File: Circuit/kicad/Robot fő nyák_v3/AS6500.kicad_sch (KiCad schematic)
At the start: 12 parts, among them U49 AS6500-FQFM, Y3 5MHz

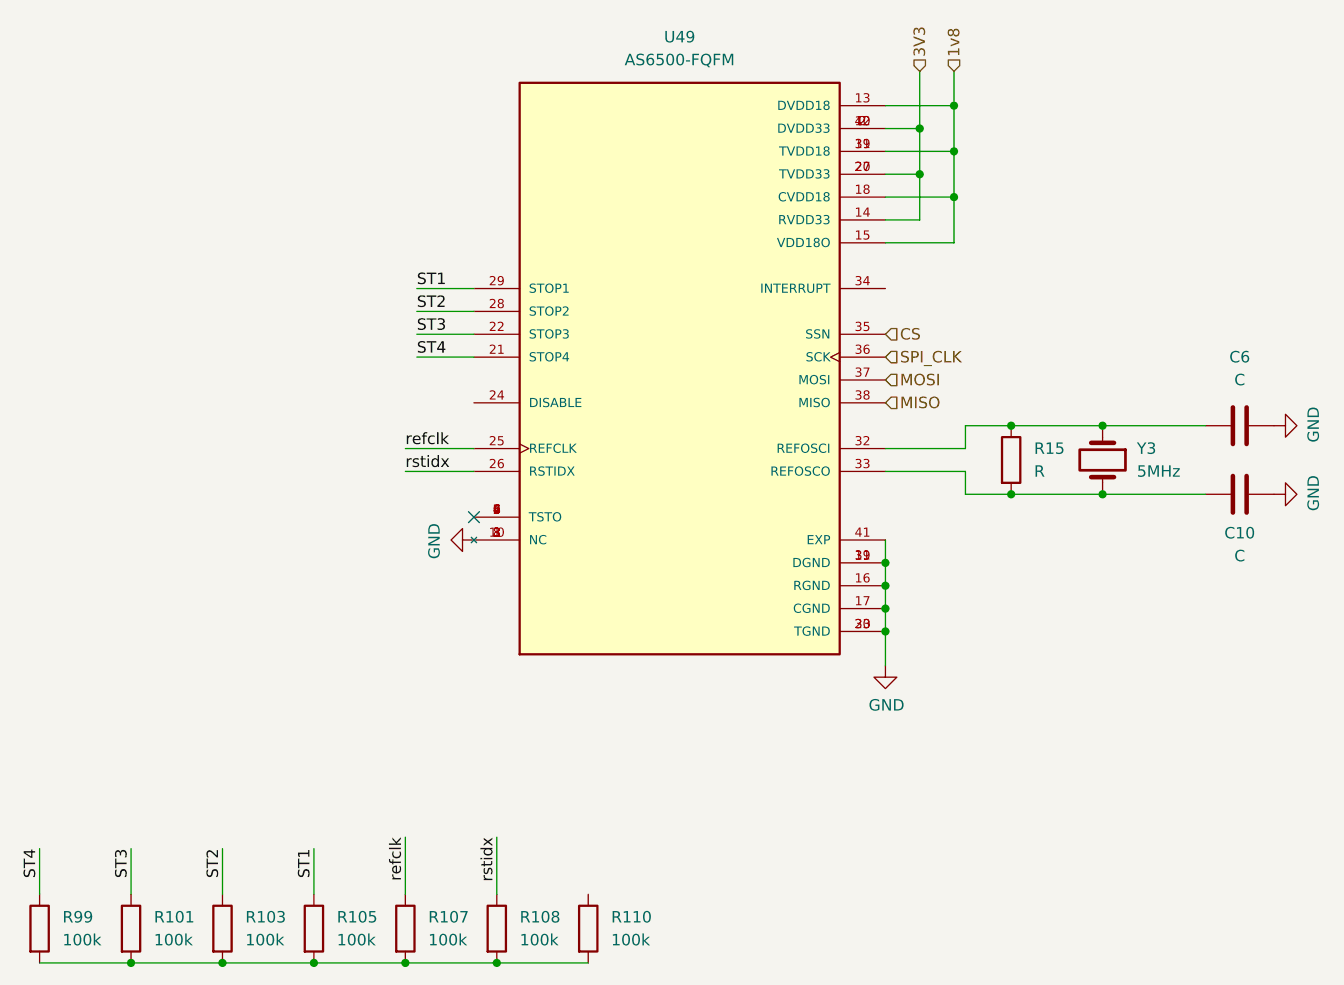
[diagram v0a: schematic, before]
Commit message: kicad v0.1 footprint- assing spi finish
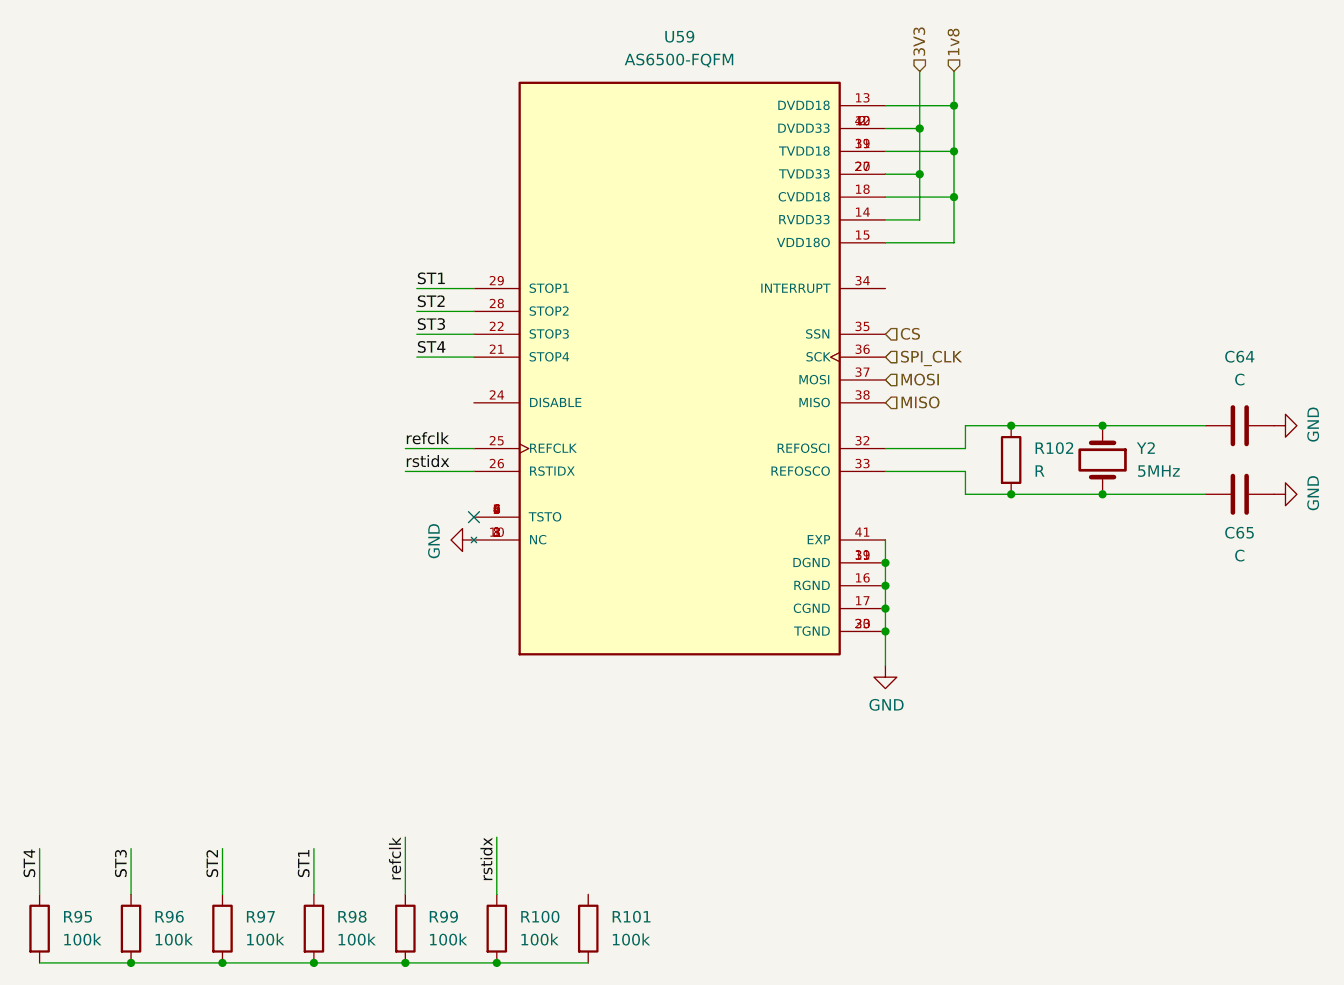
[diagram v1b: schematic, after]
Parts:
- C64: renamed from C6; footprint (none) -> Capacitor_SMD:C_0805_2012Metric
- C65: renamed from C10; footprint (none) -> Capacitor_SMD:C_0805_2012Metric
- R100: renamed from R108; footprint (none) -> Resistor_SMD:R_0805_2012Metric
- R101: renamed from R110; footprint (none) -> Resistor_SMD:R_0805_2012Metric
- R102: renamed from R15; footprint (none) -> Resistor_SMD:R_0805_2012Metric
- R95: renamed from R99; footprint (none) -> Resistor_SMD:R_0805_2012Metric
- R96: renamed from R101; footprint (none) -> Resistor_SMD:R_0805_2012Metric
- R97: renamed from R103; footprint (none) -> Resistor_SMD:R_0805_2012Metric
- R98: renamed from R105; footprint (none) -> Resistor_SMD:R_0805_2012Metric
- R99: renamed from R107; footprint (none) -> Resistor_SMD:R_0805_2012Metric
- Y2: renamed from Y3; footprint (none) -> Crystal:Crystal_SMD_HC49-SD
- renumbered U49 to U59

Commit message: kicad update new readme media updates the circuit is 95% finished
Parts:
- renumbered R102 to R100, R95 to R25, R96 to R27, R97 to R95, R98 to R96, R99 to R97, R100 to R98, R101 to R99
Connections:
- net DIS: now reaches U59.24 (DISABLE)
- no-connect marks 1 -> 2
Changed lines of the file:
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@@
+	)
+	(no_connect
+		(at 111.76 50.8)
 	)
 	(no_connect
@@
 	(wire
 		(pts
-			(xy 59.69 53.34) (xy 66.04 53.34)
+			(xy 49.53 53.34) (xy 66.04 53.34)
 		)
 		(stroke
@@
 	(wire
 		(pts
-			(xy 59.69 55.88) (xy 66.04 55.88)
+			(xy 49.53 55.88) (xy 66.04 55.88)
 		)
 		(stroke
@@
 	(wire
 		(pts
-			(xy 59.69 58.42) (xy 66.04 58.42)
+			(xy 49.53 58.42) (xy 66.04 58.42)
 		)
 		(stroke
@@
 	(wire
 		(pts
-			(xy 59.69 50.8) (xy 66.04 50.8)
+			(xy 49.53 50.8) (xy 66.04 50.8)
 		)
 		(stroke
@@
 		(pts
 			(xy 115.57 38.1) (xy 115.57 33.02)
+		)
+		(stroke
+			(width 0)
+			(type default)
+		)
+	)
+	(wire
+		(pts
+			(xy 58.42 63.5) (xy 66.04 63.5)
 		)
 		(stroke
@@
 	)
 	(label "ST2"
-		(at 59.69 53.34 0)
+		(at 49.53 53.34 0)
 		(effects
 			(font
@@
 	)
 	(label "ST3"
-		(at 59.69 55.88 0)
+		(at 49.53 55.88 0)
 		(effects
 			(font
@@
 	)
 	(label "ST1"
-		(at 59.69 50.8 0)
+		(at 49.53 50.8 0)
 		(effects
 			(font
@@
 		)
 	)
+	(label "DIS"
+		(at 58.42 63.5 0)
+		(effects
+			(font
+				(size 1.27 1.27)
+			)
+			(justify left bottom)
+		)
+	)
 	(label "ST4"
-		(at 59.69 58.42 0)
+		(at 49.53 58.42 0)
 		(effects
 			(font
@@
 		(dnp no)
 		(fields_autoplaced yes)
-		(property "Reference" "R97"
+		(property "Reference" "R95"
 			(at 40.64 120.6499 0)
 			(effects
@@
 		(instances
 			(project "CM5IO"
-				(path "/e63e39d7-6ac0-4ffd-8aa3-1841a4541b55/a83afe30-5c7e-43cb-a5b2-f6f97a0812b3/86209e6a-92ae-4699-a125-02d46b525fc7/cb22f4d7-edd9-44f2-99e1-8067511610b0"
-					(reference "R97")
+				(path "/e63e39d7-6ac0-4ffd-8aa3-1841a4541b55/a83afe30-5c7e-43cb-a5b2-f6f97a0812b3/86209e6a-92ae-4699-a125-02d46b525fc7/e7466be3-9271-431f-82f5-a7a34fd4d93a"
+					(reference "R95")
 					(unit 1)
 				)
@@
 		(instances
 			(project "CM5IO"
-				(path "/e63e39d7-6ac0-4ffd-8aa3-1841a4541b55/a83afe30-5c7e-43cb-a5b2-f6f97a0812b3/86209e6a-92ae-4699-a125-02d46b525fc7/cb22f4d7-edd9-44f2-99e1-8067511610b0"
+				(path "/e63e39d7-6ac0-4ffd-8aa3-1841a4541b55/a83afe30-5c7e-43cb-a5b2-f6f97a0812b3/86209e6a-92ae-4699-a125-02d46b525fc7/e7466be3-9271-431f-82f5-a7a34fd4d93a"
 					(reference "C65")
 					(unit 1)
@@
 		(dnp no)
 		(fields_autoplaced yes)
-		(property "Reference" "R100"
+		(property "Reference" "R98"
 			(at 71.12 120.6499 0)
 			(effects
@@
 		(instances
 			(project "CM5IO"
-				(path "/e63e39d7-6ac0-4ffd-8aa3-1841a4541b55/a83afe30-5c7e-43cb-a5b2-f6f97a0812b3/86209e6a-92ae-4699-a125-02d46b525fc7/cb22f4d7-edd9-44f2-99e1-8067511610b0"
-					(reference "R100")
+				(path "/e63e39d7-6ac0-4ffd-8aa3-1841a4541b55/a83afe30-5c7e-43cb-a5b2-f6f97a0812b3/86209e6a-92ae-4699-a125-02d46b525fc7/e7466be3-9271-431f-82f5-a7a34fd4d93a"
+					(reference "R98")
 					(unit 1)
 				)
@@
 		(dnp no)
 		(fields_autoplaced yes)
-		(property "Reference" "R102"
+		(property "Reference" "R100"
 			(at 128.27 68.5799 0)
 			(effects
@@
 		)
 		(instances
-			(project ""
-				(path "/e63e39d7-6ac0-4ffd-8aa3-1841a4541b55/a83afe30-5c7e-43cb-a5b2-f6f97a0812b3/86209e6a-92ae-4699-a125-02d46b525fc7/160ccd78-386a-4b8b-89f3-6c9a73a758a1"
-					(reference "R?")
-					(unit 1)
-				)
-				(path "/e63e39d7-6ac0-4ffd-8aa3-1841a4541b55/a83afe30-5c7e-43cb-a5b2-f6f97a0812b3/86209e6a-92ae-4699-a125-02d46b525fc7/cb22f4d7-edd9-44f2-99e1-8067511610b0"
-					(reference "R102")
+			(project "CM5IO"
+				(path "/e63e39d7-6ac0-4ffd-8aa3-1841a4541b55/a83afe30-5c7e-43cb-a5b2-f6f97a0812b3/86209e6a-92ae-4699-a125-02d46b525fc7/e7466be3-9271-431f-82f5-a7a34fd4d93a"
+					(reference "R100")
 					(unit 1)
 				)
@@
 		(dnp no)
 		(fields_autoplaced yes)
-		(property "Reference" "R101"
+		(property "Reference" "R99"
 			(at 81.28 120.6499 0)
 			(effects
@@
 		(instances
 			(project "CM5IO"
-				(path "/e63e39d7-6ac0-4ffd-8aa3-1841a4541b55/a83afe30-5c7e-43cb-a5b2-f6f97a0812b3/86209e6a-92ae-4699-a125-02d46b525fc7/cb22f4d7-edd9-44f2-99e1-8067511610b0"
-					(reference "R101")
+				(path "/e63e39d7-6ac0-4ffd-8aa3-1841a4541b55/a83afe30-5c7e-43cb-a5b2-f6f97a0812b3/86209e6a-92ae-4699-a125-02d46b525fc7/e7466be3-9271-431f-82f5-a7a34fd4d93a"
+					(reference "R99")
 					(unit 1)
 				)
@@
 		(instances
 			(project "CM5IO"
-				(path "/e63e39d7-6ac0-4ffd-8aa3-1841a4541b55/a83afe30-5c7e-43cb-a5b2-f6f97a0812b3/86209e6a-92ae-4699-a125-02d46b525fc7/cb22f4d7-edd9-44f2-99e1-8067511610b0"
+				(path "/e63e39d7-6ac0-4ffd-8aa3-1841a4541b55/a83afe30-5c7e-43cb-a5b2-f6f97a0812b3/86209e6a-92ae-4699-a125-02d46b525fc7/e7466be3-9271-431f-82f5-a7a34fd4d93a"
 					(reference "#PWR0135")
 					(unit 1)
@@
 		(instances
 			(project "CM5IO"
-				(path "/e63e39d7-6ac0-4ffd-8aa3-1841a4541b55/a83afe30-5c7e-43cb-a5b2-f6f97a0812b3/86209e6a-92ae-4699-a125-02d46b525fc7/cb22f4d7-edd9-44f2-99e1-8067511610b0"
+				(path "/e63e39d7-6ac0-4ffd-8aa3-1841a4541b55/a83afe30-5c7e-43cb-a5b2-f6f97a0812b3/86209e6a-92ae-4699-a125-02d46b525fc7/e7466be3-9271-431f-82f5-a7a34fd4d93a"
 					(reference "#PWR0134")
 					(unit 1)
@@
 		)
 		(instances
-			(project ""
-				(path "/e63e39d7-6ac0-4ffd-8aa3-1841a4541b55/a83afe30-5c7e-43cb-a5b2-f6f97a0812b3/86209e6a-92ae-4699-a125-02d46b525fc7/160ccd78-386a-4b8b-89f3-6c9a73a758a1"
-					(reference "U?")
-					(unit 1)
-				)
-				(path "/e63e39d7-6ac0-4ffd-8aa3-1841a4541b55/a83afe30-5c7e-43cb-a5b2-f6f97a0812b3/86209e6a-92ae-4699-a125-02d46b525fc7/cb22f4d7-edd9-44f2-99e1-8067511610b0"
+			(project "CM5IO"
+				(path "/e63e39d7-6ac0-4ffd-8aa3-1841a4541b55/a83afe30-5c7e-43cb-a5b2-f6f97a0812b3/86209e6a-92ae-4699-a125-02d46b525fc7/e7466be3-9271-431f-82f5-a7a34fd4d93a"
 					(reference "U59")
 					(unit 1)
@@
 		)
 		(instances
-			(project ""
-				(path "/e63e39d7-6ac0-4ffd-8aa3-1841a4541b55/a83afe30-5c7e-43cb-a5b2-f6f97a0812b3/86209e6a-92ae-4699-a125-02d46b525fc7/160ccd78-386a-4b8b-89f3-6c9a73a758a1"
-					(reference "C?")
-					(unit 1)
-				)
-				(path "/e63e39d7-6ac0-4ffd-8aa3-1841a4541b55/a83afe30-5c7e-43cb-a5b2-f6f97a0812b3/86209e6a-92ae-4699-a125-02d46b525fc7/cb22f4d7-edd9-44f2-99e1-8067511610b0"
+			(project "CM5IO"
+				(path "/e63e39d7-6ac0-4ffd-8aa3-1841a4541b55/a83afe30-5c7e-43cb-a5b2-f6f97a0812b3/86209e6a-92ae-4699-a125-02d46b525fc7/e7466be3-9271-431f-82f5-a7a34fd4d93a"
 					(reference "C64")
 					(unit 1)
@@
 		(dnp no)
 		(fields_autoplaced yes)
-		(property "Reference" "R95"
+		(property "Reference" "R25"
 			(at 20.32 120.6499 0)
 			(effects
@@
 		(instances
 			(project "CM5IO"
-				(path "/e63e39d7-6ac0-4ffd-8aa3-1841a4541b55/a83afe30-5c7e-43cb-a5b2-f6f97a0812b3/86209e6a-92ae-4699-a125-02d46b525fc7/cb22f4d7-edd9-44f2-99e1-8067511610b0"
-					(reference "R95")
+				(path "/e63e39d7-6ac0-4ffd-8aa3-1841a4541b55/a83afe30-5c7e-43cb-a5b2-f6f97a0812b3/86209e6a-92ae-4699-a125-02d46b525fc7/e7466be3-9271-431f-82f5-a7a34fd4d93a"
+					(reference "R25")
 					(unit 1)
 				)
@@
 		(dnp no)
 		(fields_autoplaced yes)
-		(property "Reference" "R99"
+		(property "Reference" "R97"
 			(at 60.96 120.6499 0)
 			(effects
@@
 		(instances
 			(project "CM5IO"
-				(path "/e63e39d7-6ac0-4ffd-8aa3-1841a4541b55/a83afe30-5c7e-43cb-a5b2-f6f97a0812b3/86209e6a-92ae-4699-a125-02d46b525fc7/cb22f4d7-edd9-44f2-99e1-8067511610b0"
-					(reference "R99")
+				(path "/e63e39d7-6ac0-4ffd-8aa3-1841a4541b55/a83afe30-5c7e-43cb-a5b2-f6f97a0812b3/86209e6a-92ae-4699-a125-02d46b525fc7/e7466be3-9271-431f-82f5-a7a34fd4d93a"
+					(reference "R97")
 					(unit 1)
 				)
@@
 		(dnp no)
 		(fields_autoplaced yes)
-		(property "Reference" "R98"
+		(property "Reference" "R96"
 			(at 50.8 120.6499 0)
 			(effects
@@
 		(instances
 			(project "CM5IO"
-				(path "/e63e39d7-6ac0-4ffd-8aa3-1841a4541b55/a83afe30-5c7e-43cb-a5b2-f6f97a0812b3/86209e6a-92ae-4699-a125-02d46b525fc7/cb22f4d7-edd9-44f2-99e1-8067511610b0"
-					(reference "R98")
+				(path "/e63e39d7-6ac0-4ffd-8aa3-1841a4541b55/a83afe30-5c7e-43cb-a5b2-f6f97a0812b3/86209e6a-92ae-4699-a125-02d46b525fc7/e7466be3-9271-431f-82f5-a7a34fd4d93a"
+					(reference "R96")
 					(unit 1)
 				)
@@
 		)
 		(instances
-			(project ""
-				(path "/e63e39d7-6ac0-4ffd-8aa3-1841a4541b55/a83afe30-5c7e-43cb-a5b2-f6f97a0812b3/86209e6a-92ae-4699-a125-02d46b525fc7/160ccd78-386a-4b8b-89f3-6c9a73a758a1"
-					(reference "Y?")
-					(unit 1)
-				)
-				(path "/e63e39d7-6ac0-4ffd-8aa3-1841a4541b55/a83afe30-5c7e-43cb-a5b2-f6f97a0812b3/86209e6a-92ae-4699-a125-02d46b525fc7/cb22f4d7-edd9-44f2-99e1-8067511610b0"
+			(project "CM5IO"
+				(path "/e63e39d7-6ac0-4ffd-8aa3-1841a4541b55/a83afe30-5c7e-43cb-a5b2-f6f97a0812b3/86209e6a-92ae-4699-a125-02d46b525fc7/e7466be3-9271-431f-82f5-a7a34fd4d93a"
 					(reference "Y2")
 					(unit 1)
@@
 		(dnp no)
 		(fields_autoplaced yes)
-		(property "Reference" "R96"
+		(property "Reference" "R27"
 			(at 30.48 120.6499 0)
 			(effects
@@
 		(instances
 			(project "CM5IO"
-				(path "/e63e39d7-6ac0-4ffd-8aa3-1841a4541b55/a83afe30-5c7e-43cb-a5b2-f6f97a0812b3/86209e6a-92ae-4699-a125-02d46b525fc7/cb22f4d7-edd9-44f2-99e1-8067511610b0"
-					(reference "R96")
+				(path "/e63e39d7-6ac0-4ffd-8aa3-1841a4541b55/a83afe30-5c7e-43cb-a5b2-f6f97a0812b3/86209e6a-92ae-4699-a125-02d46b525fc7/e7466be3-9271-431f-82f5-a7a34fd4d93a"
+					(reference "R27")
 					(unit 1)
 				)
@@
 		(instances
 			(project "CM5IO"
-				(path "/e63e39d7-6ac0-4ffd-8aa3-1841a4541b55/a83afe30-5c7e-43cb-a5b2-f6f97a0812b3/86209e6a-92ae-4699-a125-02d46b525fc7/cb22f4d7-edd9-44f2-99e1-8067511610b0"
+				(path "/e63e39d7-6ac0-4ffd-8aa3-1841a4541b55/a83afe30-5c7e-43cb-a5b2-f6f97a0812b3/86209e6a-92ae-4699-a125-02d46b525fc7/e7466be3-9271-431f-82f5-a7a34fd4d93a"
 					(reference "#PWR0137")
 					(unit 1)
@@
 		(instances
 			(project "CM5IO"
-				(path "/e63e39d7-6ac0-4ffd-8aa3-1841a4541b55/a83afe30-5c7e-43cb-a5b2-f6f97a0812b3/86209e6a-92ae-4699-a125-02d46b525fc7/cb22f4d7-edd9-44f2-99e1-8067511610b0"
+				(path "/e63e39d7-6ac0-4ffd-8aa3-1841a4541b55/a83afe30-5c7e-43cb-a5b2-f6f97a0812b3/86209e6a-92ae-4699-a125-02d46b525fc7/e7466be3-9271-431f-82f5-a7a34fd4d93a"
 					(reference "#PWR0136")
 					(unit 1)

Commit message: readme updated kicad circuit V1
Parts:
- renumbered C64 to C114, C65 to C115, R97 to R100, R98 to R101, R99 to R102, R100 to R103, R25 to R96, R27 to R97, R95 to R98, R96 to R99, U59 to U58
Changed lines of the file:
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@@
 		(dnp no)
 		(fields_autoplaced yes)
-		(property "Reference" "R95"
+		(property "Reference" "R98"
 			(at 40.64 120.6499 0)
 			(effects
@@
 			(project "CM5IO"
 				(path "/e63e39d7-6ac0-4ffd-8aa3-1841a4541b55/a83afe30-5c7e-43cb-a5b2-f6f97a0812b3/86209e6a-92ae-4699-a125-02d46b525fc7/e7466be3-9271-431f-82f5-a7a34fd4d93a"
-					(reference "R95")
+					(reference "R98")
 					(unit 1)
 				)
@@
 		(on_board yes)
 		(dnp no)
-		(property "Reference" "C65"
+		(property "Reference" "C115"
 			(at 151.13 77.978 90)
 			(effects
@@
 			(project "CM5IO"
 				(path "/e63e39d7-6ac0-4ffd-8aa3-1841a4541b55/a83afe30-5c7e-43cb-a5b2-f6f97a0812b3/86209e6a-92ae-4699-a125-02d46b525fc7/e7466be3-9271-431f-82f5-a7a34fd4d93a"
-					(reference "C65")
+					(reference "C115")
 					(unit 1)
 				)
@@
 		(dnp no)
 		(fields_autoplaced yes)
-		(property "Reference" "R98"
+		(property "Reference" "R101"
 			(at 71.12 120.6499 0)
 			(effects
@@
 			(project "CM5IO"
 				(path "/e63e39d7-6ac0-4ffd-8aa3-1841a4541b55/a83afe30-5c7e-43cb-a5b2-f6f97a0812b3/86209e6a-92ae-4699-a125-02d46b525fc7/e7466be3-9271-431f-82f5-a7a34fd4d93a"
-					(reference "R98")
+					(reference "R101")
 					(unit 1)
 				)
@@
 		(dnp no)
 		(fields_autoplaced yes)
-		(property "Reference" "R100"
+		(property "Reference" "R103"
 			(at 128.27 68.5799 0)
 			(effects
@@
 			(project "CM5IO"
 				(path "/e63e39d7-6ac0-4ffd-8aa3-1841a4541b55/a83afe30-5c7e-43cb-a5b2-f6f97a0812b3/86209e6a-92ae-4699-a125-02d46b525fc7/e7466be3-9271-431f-82f5-a7a34fd4d93a"
-					(reference "R100")
+					(reference "R103")
 					(unit 1)
 				)
@@
 		(dnp no)
 		(fields_autoplaced yes)
-		(property "Reference" "R99"
+		(property "Reference" "R102"
 			(at 81.28 120.6499 0)
 			(effects
@@
 			(project "CM5IO"
 				(path "/e63e39d7-6ac0-4ffd-8aa3-1841a4541b55/a83afe30-5c7e-43cb-a5b2-f6f97a0812b3/86209e6a-92ae-4699-a125-02d46b525fc7/e7466be3-9271-431f-82f5-a7a34fd4d93a"
-					(reference "R99")
+					(reference "R102")
 					(unit 1)
 				)
@@
 		(on_board yes)
 		(dnp no)
-		(property "Reference" "#PWR0135"
+		(property "Reference" "#PWR0157"
 			(at 111.76 99.06 0)
 			(effects
@@
 			(project "CM5IO"
 				(path "/e63e39d7-6ac0-4ffd-8aa3-1841a4541b55/a83afe30-5c7e-43cb-a5b2-f6f97a0812b3/86209e6a-92ae-4699-a125-02d46b525fc7/e7466be3-9271-431f-82f5-a7a34fd4d93a"
-					(reference "#PWR0135")
+					(reference "#PWR0157")
 					(unit 1)
 				)
@@
 		(on_board yes)
 		(dnp no)
-		(property "Reference" "#PWR0134"
+		(property "Reference" "#PWR0156"
 			(at 59.69 78.74 0)
 			(effects
@@
 			(project "CM5IO"
 				(path "/e63e39d7-6ac0-4ffd-8aa3-1841a4541b55/a83afe30-5c7e-43cb-a5b2-f6f97a0812b3/86209e6a-92ae-4699-a125-02d46b525fc7/e7466be3-9271-431f-82f5-a7a34fd4d93a"
-					(reference "#PWR0134")
+					(reference "#PWR0156")
 					(unit 1)
 				)
@@
 		(dnp no)
 		(fields_autoplaced yes)
-		(property "Reference" "U59"
+		(property "Reference" "U58"
 			(at 88.9 22.86 0)
 			(effects
@@
 			(project "CM5IO"
 				(path "/e63e39d7-6ac0-4ffd-8aa3-1841a4541b55/a83afe30-5c7e-43cb-a5b2-f6f97a0812b3/86209e6a-92ae-4699-a125-02d46b525fc7/e7466be3-9271-431f-82f5-a7a34fd4d93a"
-					(reference "U59")
+					(reference "U58")
 					(unit 1)
 				)
@@
 		(dnp no)
 		(fields_autoplaced yes)
-		(property "Reference" "C64"
+		(property "Reference" "C114"
 			(at 151.13 58.42 90)
 			(effects
@@
 			(project "CM5IO"
 				(path "/e63e39d7-6ac0-4ffd-8aa3-1841a4541b55/a83afe30-5c7e-43cb-a5b2-f6f97a0812b3/86209e6a-92ae-4699-a125-02d46b525fc7/e7466be3-9271-431f-82f5-a7a34fd4d93a"
-					(reference "C64")
+					(reference "C114")
 					(unit 1)
 				)
@@
 		(dnp no)
 		(fields_autoplaced yes)
-		(property "Reference" "R25"
+		(property "Reference" "R96"
 			(at 20.32 120.6499 0)
 			(effects
@@
 			(project "CM5IO"
 				(path "/e63e39d7-6ac0-4ffd-8aa3-1841a4541b55/a83afe30-5c7e-43cb-a5b2-f6f97a0812b3/86209e6a-92ae-4699-a125-02d46b525fc7/e7466be3-9271-431f-82f5-a7a34fd4d93a"
-					(reference "R25")
+					(reference "R96")
 					(unit 1)
 				)
@@
 		(dnp no)
 		(fields_autoplaced yes)
-		(property "Reference" "R97"
+		(property "Reference" "R100"
 			(at 60.96 120.6499 0)
 			(effects
@@
 			(project "CM5IO"
 				(path "/e63e39d7-6ac0-4ffd-8aa3-1841a4541b55/a83afe30-5c7e-43cb-a5b2-f6f97a0812b3/86209e6a-92ae-4699-a125-02d46b525fc7/e7466be3-9271-431f-82f5-a7a34fd4d93a"
-					(reference "R97")
+					(reference "R100")
 					(unit 1)
 				)
@@
 		(dnp no)
 		(fields_autoplaced yes)
-		(property "Reference" "R96"
+		(property "Reference" "R99"
 			(at 50.8 120.6499 0)
 			(effects
@@
 			(project "CM5IO"
 				(path "/e63e39d7-6ac0-4ffd-8aa3-1841a4541b55/a83afe30-5c7e-43cb-a5b2-f6f97a0812b3/86209e6a-92ae-4699-a125-02d46b525fc7/e7466be3-9271-431f-82f5-a7a34fd4d93a"
-					(reference "R96")
+					(reference "R99")
 					(unit 1)
 				)
@@
 		(dnp no)
 		(fields_autoplaced yes)
-		(property "Reference" "R27"
+		(property "Reference" "R97"
 			(at 30.48 120.6499 0)
 			(effects
@@
 			(project "CM5IO"
 				(path "/e63e39d7-6ac0-4ffd-8aa3-1841a4541b55/a83afe30-5c7e-43cb-a5b2-f6f97a0812b3/86209e6a-92ae-4699-a125-02d46b525fc7/e7466be3-9271-431f-82f5-a7a34fd4d93a"
-					(reference "R27")
+					(reference "R97")
 					(unit 1)
 				)
@@
 		(on_board yes)
 		(dnp no)
-		(property "Reference" "#PWR0137"
+		(property "Reference" "#PWR0159"
 			(at 161.29 73.66 0)
 			(effects
@@
 			(project "CM5IO"
 				(path "/e63e39d7-6ac0-4ffd-8aa3-1841a4541b55/a83afe30-5c7e-43cb-a5b2-f6f97a0812b3/86209e6a-92ae-4699-a125-02d46b525fc7/e7466be3-9271-431f-82f5-a7a34fd4d93a"
-					(reference "#PWR0137")
+					(reference "#PWR0159")
 					(unit 1)
 				)
@@
 		(on_board yes)
 		(dnp no)
-		(property "Reference" "#PWR0136"
+		(property "Reference" "#PWR0158"
 			(at 161.29 66.04 0)
 			(effects
@@
 			(project "CM5IO"
 				(path "/e63e39d7-6ac0-4ffd-8aa3-1841a4541b55/a83afe30-5c7e-43cb-a5b2-f6f97a0812b3/86209e6a-92ae-4699-a125-02d46b525fc7/e7466be3-9271-431f-82f5-a7a34fd4d93a"
-					(reference "#PWR0136")
-					(unit 1)
-				)
+					(reference "#PWR0158")
+					(unit 1)
+				)
